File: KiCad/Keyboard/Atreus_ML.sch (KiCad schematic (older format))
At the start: 85 parts

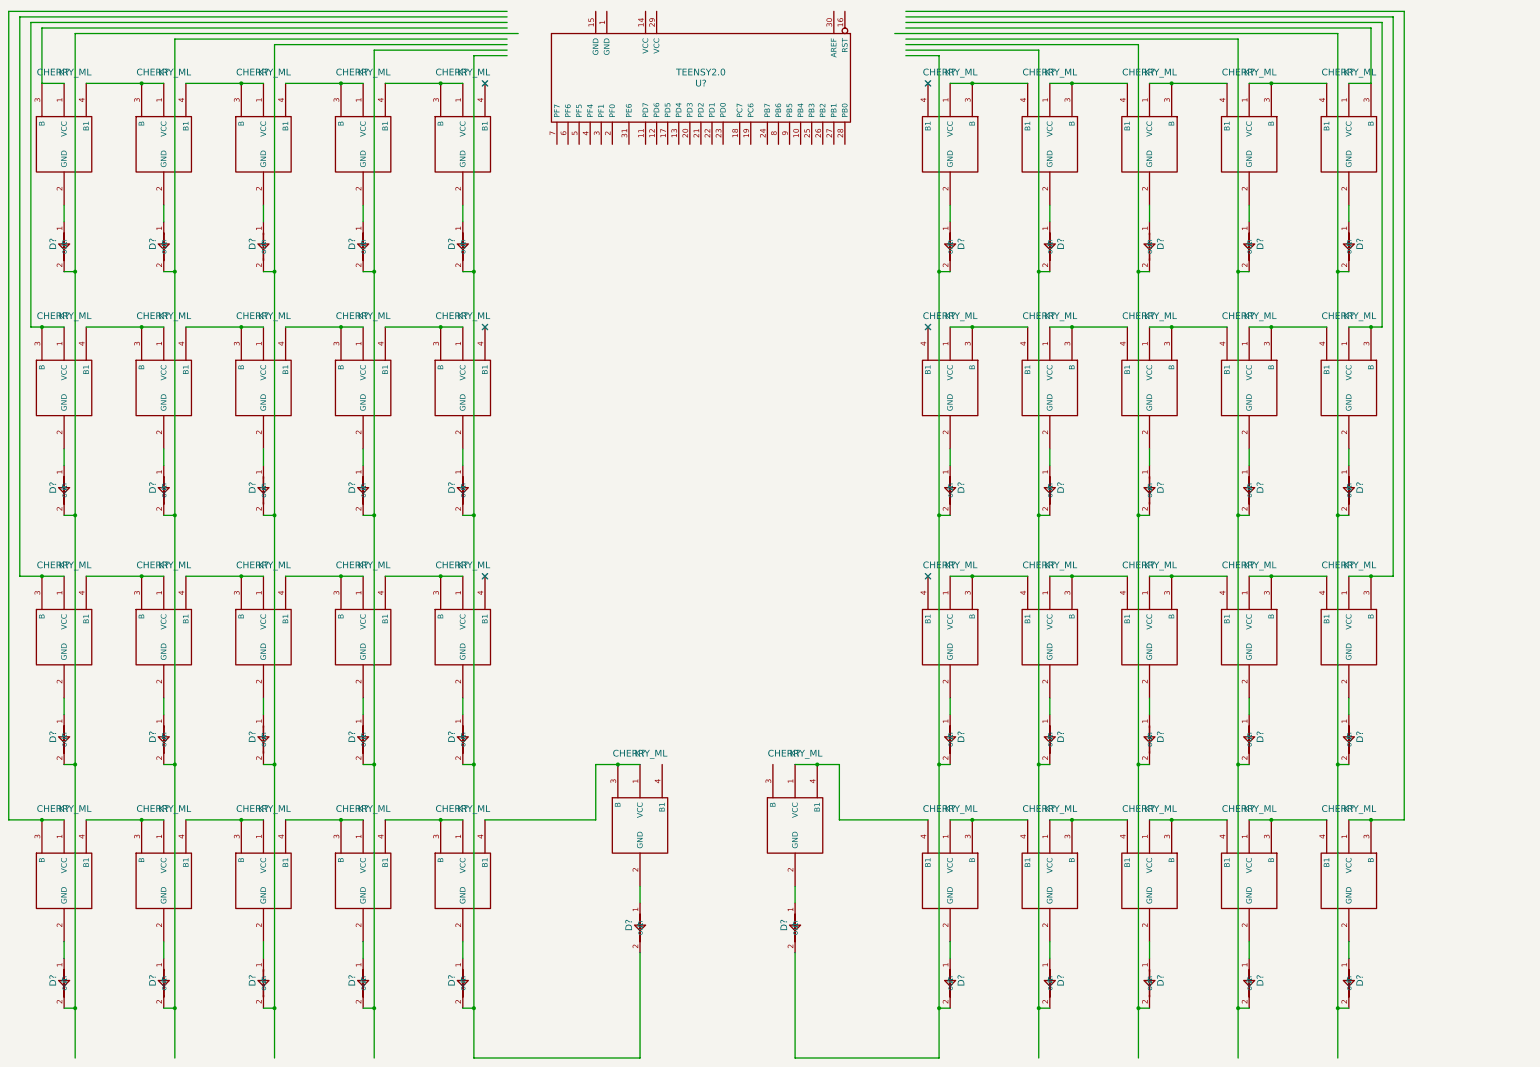
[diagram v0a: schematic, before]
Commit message: First draft of schematic digram
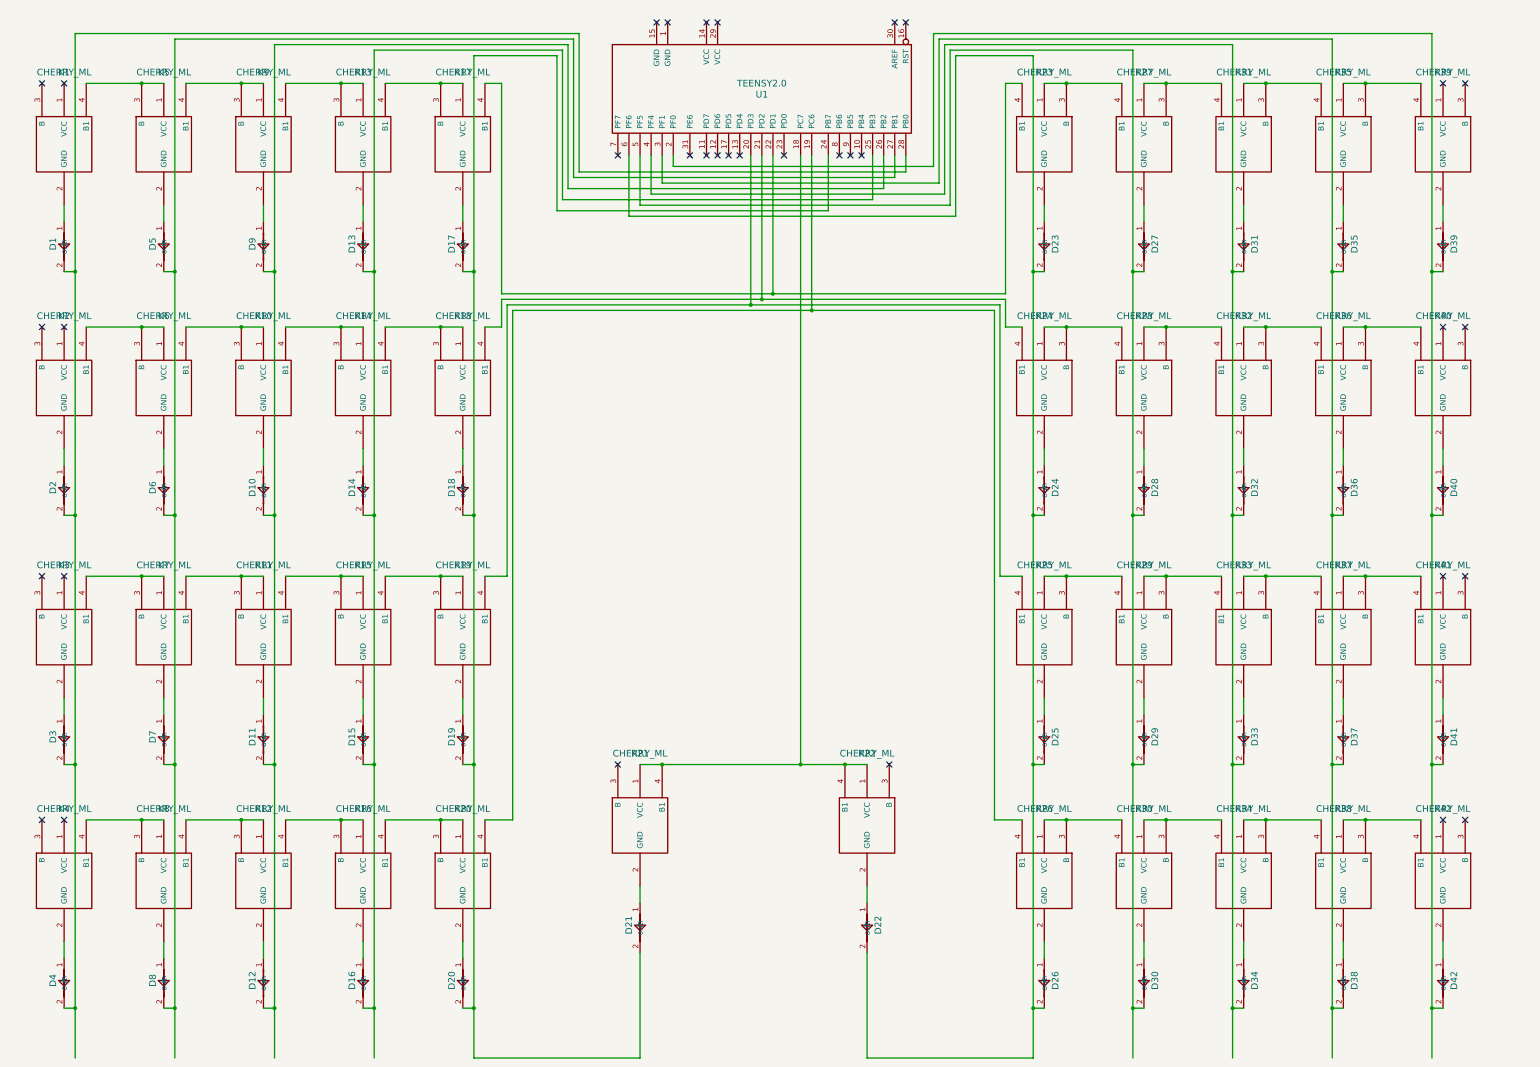
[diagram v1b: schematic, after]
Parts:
- removed D? (x21): 4148, symbol 4148
- removed K? (x21): CHERRY_ML, symbol CHERRY_ML
- added D22, D23, D24, D25, D26, D27, D28, D29, D30, D31, D32, D33, D34, D35, D36, D37, D38, D39, D40, D41, D42: 4148, symbol 4148
- added K22, K23, K24, K25, K26, K27, K28, K29, K30, K31, K32, K33, K34, K35, K36, K37, K38, K39, K40, K41, K42: CHERRY_ML, symbol CHERRY_ML
- gave numbers to parts that had none: 43
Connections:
- wire segments 168 -> 194
- no-connect marks 6 -> 34
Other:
- moved on the sheet: U1

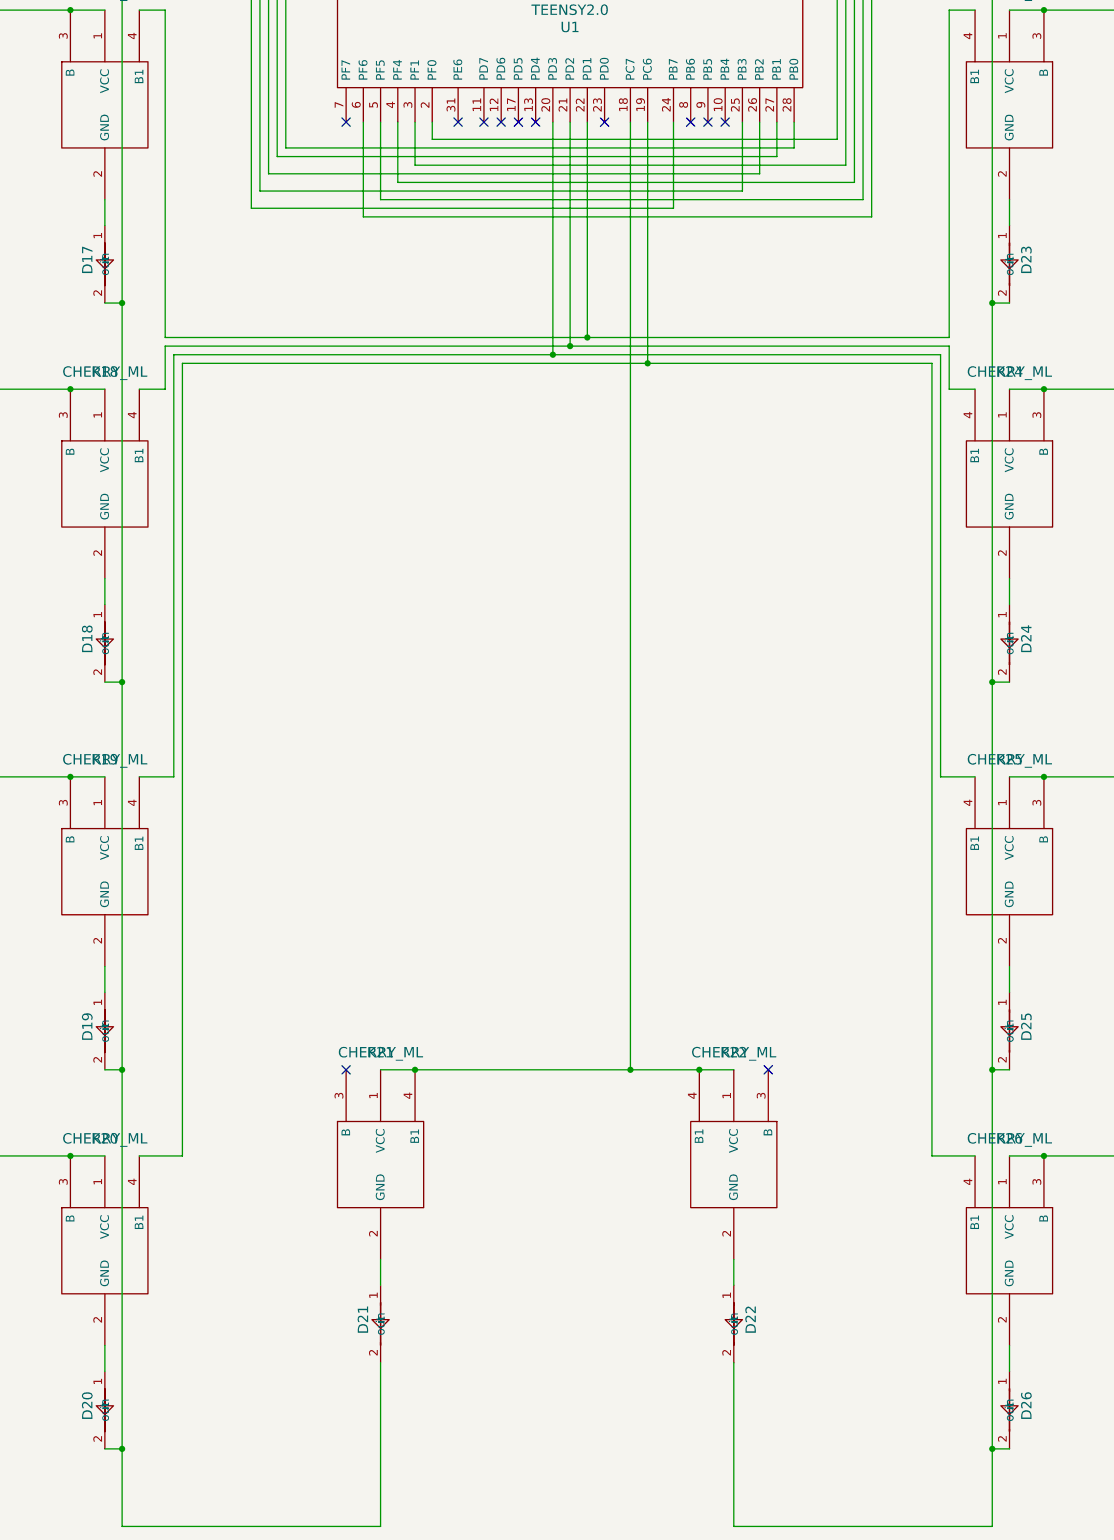
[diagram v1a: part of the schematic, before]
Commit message: Redoing lost work: Removing stopid modifier keys as single row
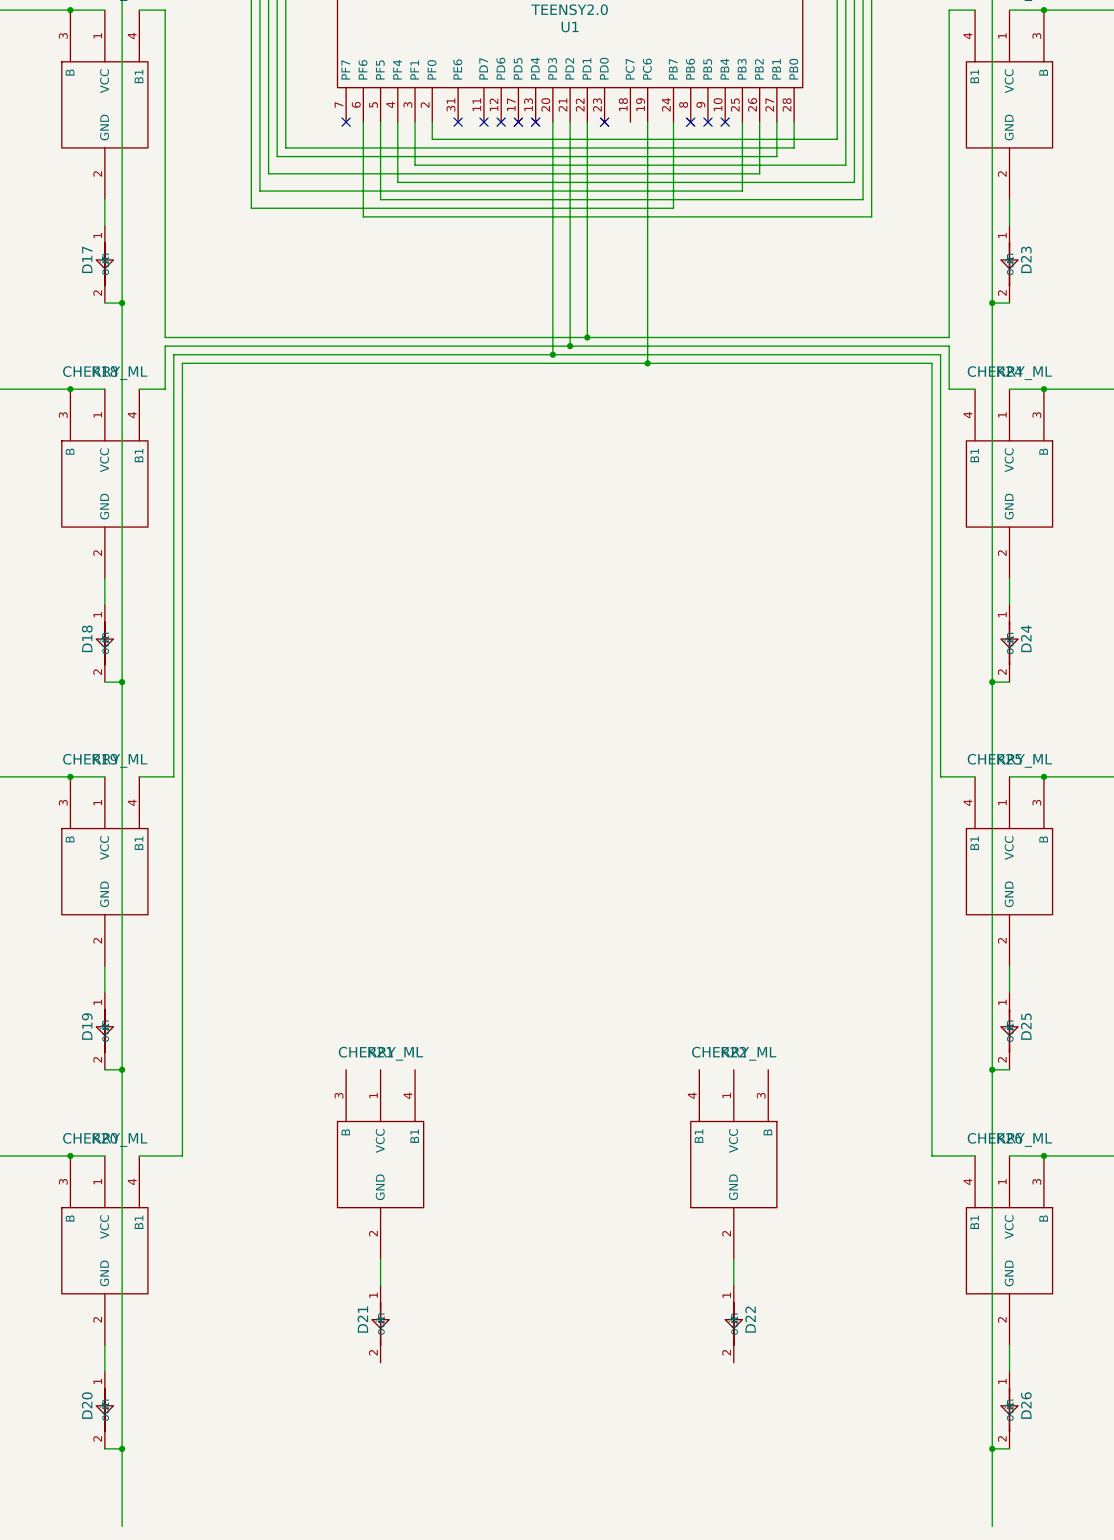
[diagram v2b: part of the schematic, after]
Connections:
- wire segments 194 -> 188
- no-connect marks 34 -> 32
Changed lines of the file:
@@
 LIBS:contrib
 LIBS:valves
-LIBS:4148_rev2
-LIBS:cherry_ml
 LIBS:components
 LIBS:Atreus_ML-cache
-EELAYER 25 0
+EELAYER 27 0
 EELAYER END
 $Descr A3 16535 11693
@@
 Sheet 1 1
 Title ""
-Date ""
+Date "21 mar 2016"
 Rev ""
 Comp ""
@@
 Connection ~ 5550 7850
 Wire Wire Line
-	5850 10000 7350 10000
-Wire Wire Line
-	7350 10000 7350 9050
-Wire Wire Line
 	5950 1200 6100 1200
 Wire Wire Line
@@
 $EndComp
 $Comp
-L CHERRY_ML K22
-U 1 1 56DF7362
-P 9400 7250
-F 0 "K22" H 9400 7250 60  0000 C CNN
-F 1 "CHERRY_ML" H 9400 7250 60  0000 C CNN
-F 2 "" H 9400 7250 60  0000 C CNN
-F 3 "" H 9400 7250 60  0000 C CNN
-	1    9400 7250
-	-1   0    0    -1
-$EndComp
-$Comp
 L 4148 D22
 U 1 1 56DF7368
@@
 Connection ~ 11200 7850
 Wire Wire Line
-	10900 10000 9400 10000
-Wire Wire Line
-	9400 10000 9400 9050
-Wire Wire Line
 	10800 1200 10650 1200
 Wire Wire Line
@@
 	10550 7850 10800 7850
 Wire Wire Line
-	7350 7350 9400 7350
-Connection ~ 7550 7350
-Connection ~ 9200 7350
-Wire Wire Line
 	9750 1850 9750 2000
 Wire Wire Line
@@
 Wire Wire Line
 	7250 2400 7250 1850
-Wire Wire Line
-	8800 1850 8800 7350
-Connection ~ 8800 7350
 Wire Wire Line
 	8900 1850 8900 3250
@@
 NoConn ~ 1950 1200
 NoConn ~ 2150 1200
-NoConn ~ 9600 7350
-NoConn ~ 7150 7350
 NoConn ~ 8650 1850
 NoConn ~ 9150 1850
@@
 NoConn ~ 7600 650
 NoConn ~ 7500 650
+$Comp
+L CHERRY_ML K22
+U 1 1 56DF7362
+P 9400 7250
+F 0 "K22" H 9400 7250 60  0000 C CNN
+F 1 "CHERRY_ML" H 9400 7250 60  0000 C CNN
+F 2 "" H 9400 7250 60  0000 C CNN
+F 3 "" H 9400 7250 60  0000 C CNN
+	1    9400 7250
+	-1   0    0    -1
+$EndComp
 $EndSCHEMATC

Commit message: Netlist
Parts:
- added P1: CONN_01X07, symbol CONN_01X07
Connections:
- wire segments 188 -> 215
- no-connect marks 32 -> 29
